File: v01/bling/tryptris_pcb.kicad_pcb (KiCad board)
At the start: 2 copper layers, 298.8 x 122 mm, 217 parts, among them J1 USB_C_Receptacle_USB2.0, J2 I2C-L, J3 I2C-R, SW1 Reset, U1 ATmega32U4-AU, U2 MCP23017_SO, U3 IS31FL3733-TQ, U4 HOLE, U4 IS31FL3733-TQ, Y1 16Mhz

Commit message: Add RGB specific silk screens
Don't want to silkscreen over the RGB holes. Also remove some cruft.
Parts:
- removed the G*** at (100.2, 88.0)
- added G***: LOGO, v01:constellation-right-rgb, B.Cu at (251.4, 88.2)
- added G***: LOGO, v01:constellation-left-rgb, B.Cu at (100.5, 88.5)
- moved G*** 152.1 mm to (398.4, 125.7)

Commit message: Remove redundant silk screen.
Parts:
- removed the G*** at (398.4, 125.7)

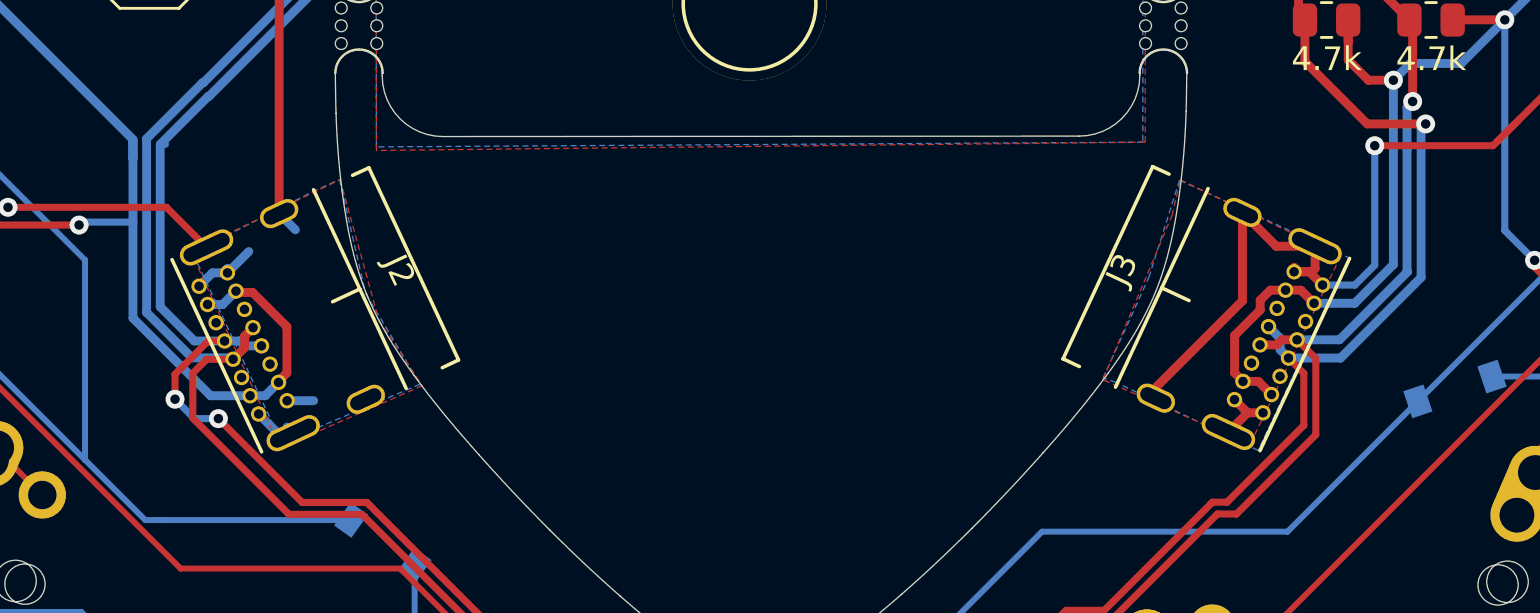
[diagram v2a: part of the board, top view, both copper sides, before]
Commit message: Move interconnect ports
I got some feedback that they might be tight for some cables. By sliding
the ports down a bit they can stay at the same angle and also give more
space for cable housing.
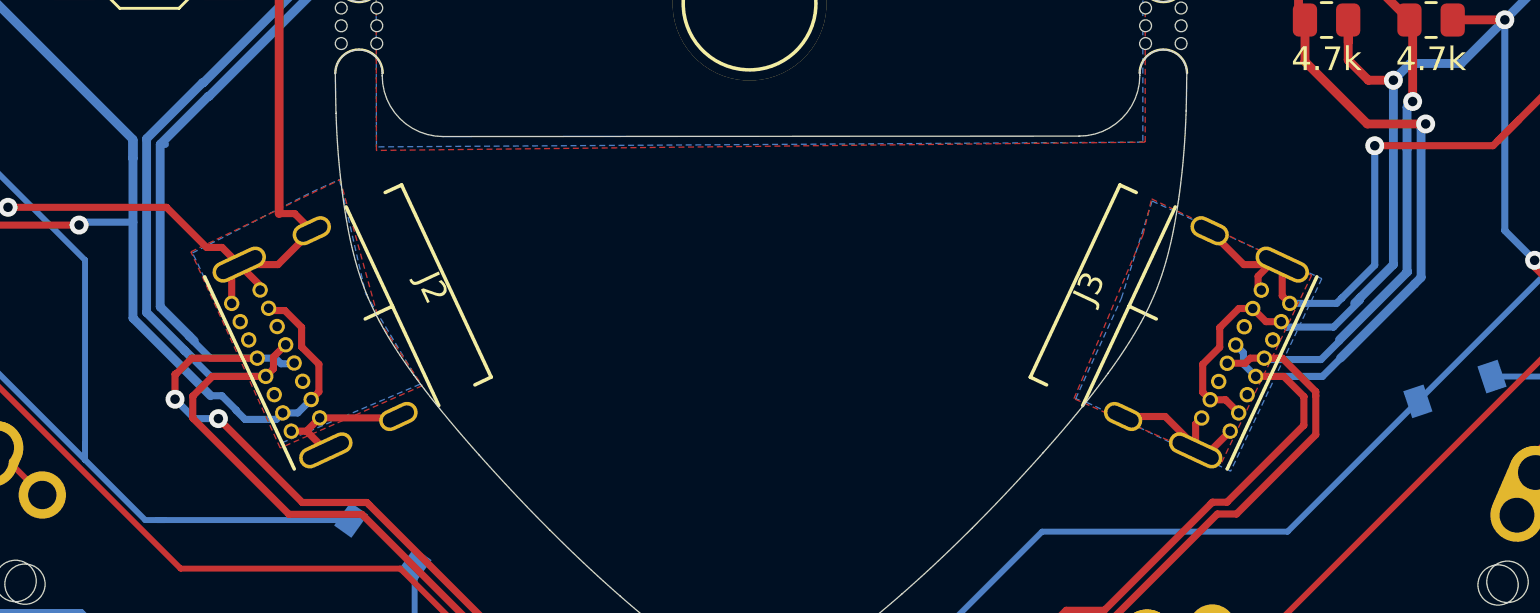
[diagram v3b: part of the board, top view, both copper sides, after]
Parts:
- moved J3 1.59 mm to (191.5, 114.5)
- moved J2 1.56 mm to (160.4, 114.5)
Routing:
- net GND: track 305.6 -> 314.6 mm
- net VSS: track 205.6 -> 202.5 mm
- net SCL-L: track 171.3 -> 174.3 mm
- net SDA-L: track 161.7 -> 164.2 mm
- net VBUS: track 217.4 -> 219.6 mm
- net SCL-R: track 163.2 -> 165.4 mm
- net SDA-R: track 154.0 -> 156.1 mm

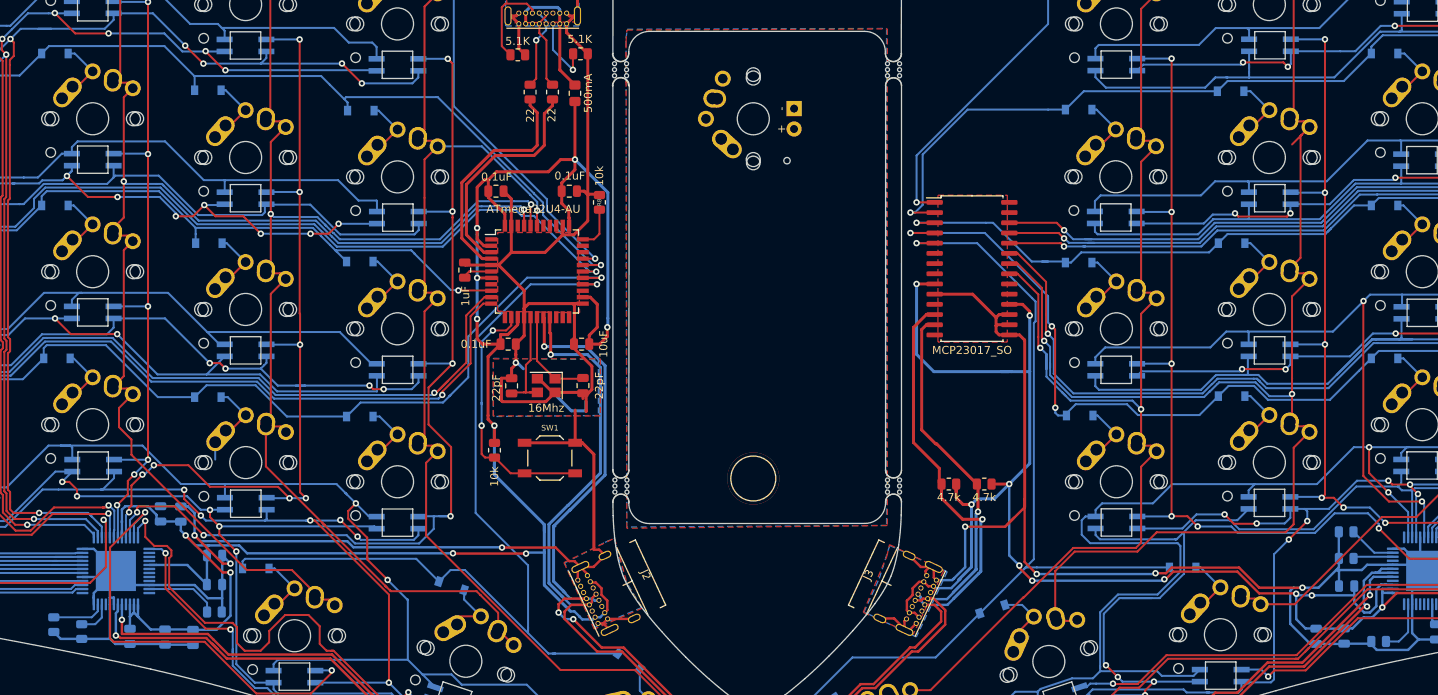
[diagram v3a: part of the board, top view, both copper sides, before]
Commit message: Move RGB LED footprint to a local lib
I don't want as much content on the silkscreen.
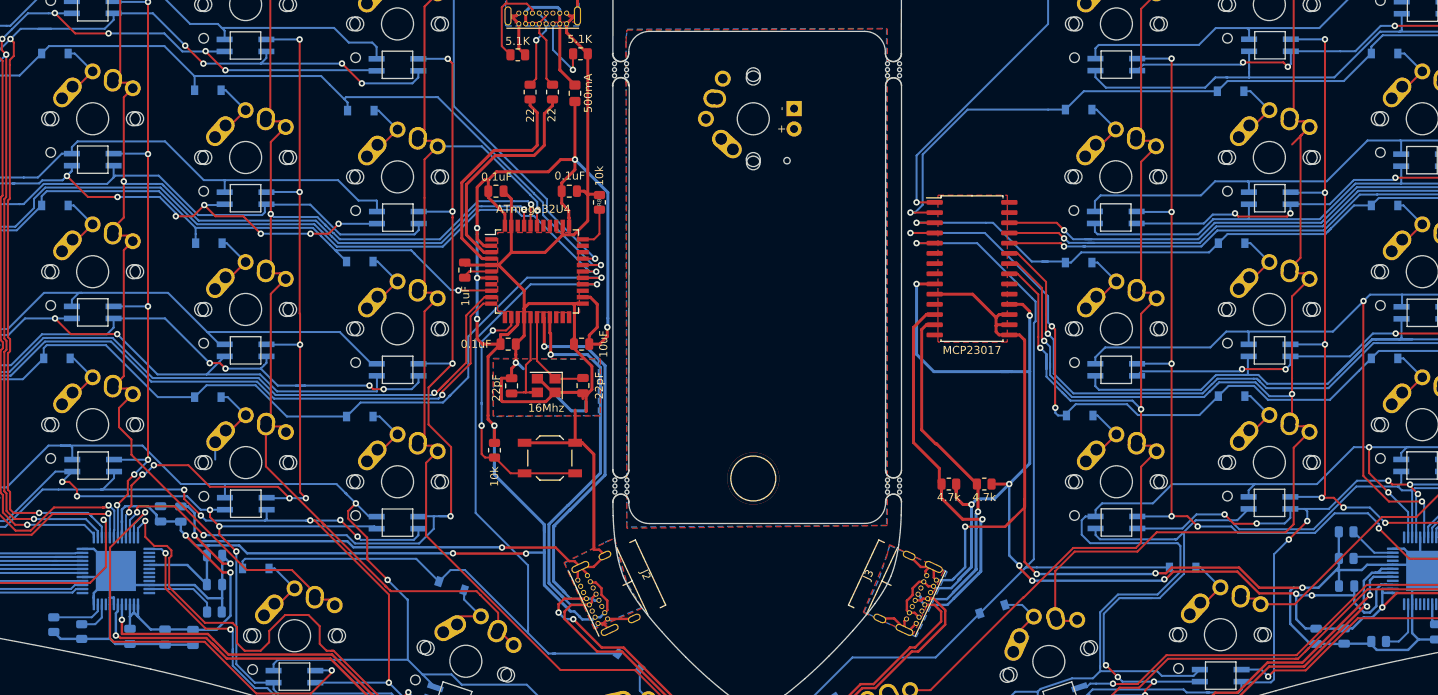
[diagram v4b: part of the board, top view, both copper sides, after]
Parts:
- D100, D101, D102, D103, D104, D105, D106, D107, D108, D55, D56, D57, D58, D59, D60, D61, D62, D63, D64, D65, D66, D67, D68, D69, D70, D71, D72, D73, D74, D75, D76, D77, D78, D79, D80, D81, D82, D83, D84, D85, D86, D87, D88, D89, D90, D91, D92, D93, D94, D95, D96, D97, D98, D99: footprint Keebio-Parts:RGB_3528_Blue_Notch-MX -> v01:RGB_3528_Blue_Notch-MX
- U1: value ATmega32U4-AU -> ATmega32U4
- U2: value MCP23017_SO -> MCP23017

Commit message: Add mounting holes to bling.
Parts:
- added REF**: MountingHole_2.2mm_M2_DIN965_Pad, MountingHole:MountingHole_2.2mm_M2_DIN965_Pad, F.Cu at (161.9, 123.0)
- added REF**: MountingHole_2.2mm_M2_DIN965_Pad, MountingHole:MountingHole_2.2mm_M2_DIN965_Pad, F.Cu at (190.2, 123.1)
- added REF**: MountingHole_2.2mm_M2_DIN965_Pad, MountingHole:MountingHole_2.2mm_M2_DIN965_Pad, F.Cu at (208.9, 54.6)
- added REF**: MountingHole_2.2mm_M2_DIN965_Pad, MountingHole:MountingHole_2.2mm_M2_DIN965_Pad, F.Cu at (143.0, 54.6)
- added REF**: MountingHole_2.2mm_M2_DIN965_Pad, MountingHole:MountingHole_2.2mm_M2_DIN965_Pad, F.Cu at (268.5, 118.8)
- added REF**: MountingHole_2.2mm_M2_DIN965_Pad, MountingHole:MountingHole_2.2mm_M2_DIN965_Pad, F.Cu at (83.8, 118.8)
- added REF**: MountingHole_2.2mm_M2_DIN965_Pad, MountingHole:MountingHole_2.2mm_M2_DIN965_Pad, F.Cu at (306.3, 37.6)
- added REF**: MountingHole_2.2mm_M2_DIN965_Pad, MountingHole:MountingHole_2.2mm_M2_DIN965_Pad, F.Cu at (45.7, 37.5)
- moved D27 9.36 mm to (167.5, 130.0)
- moved C9 5.27 mm to (273.2, 117.4)
- moved C15 5.27 mm to (276.6, 117.4)
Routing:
- net VBUS: track 219.6 -> 232.5 mm, vias 14 -> 12
- net Row4-L: track 113.4 -> 124.1 mm
- net VSS: track 202.5 -> 210.6 mm
- net Net-(D27-Pad2): track 9.48 -> 12.5 mm
- net Row1-R: track 141.1 -> 142.2 mm

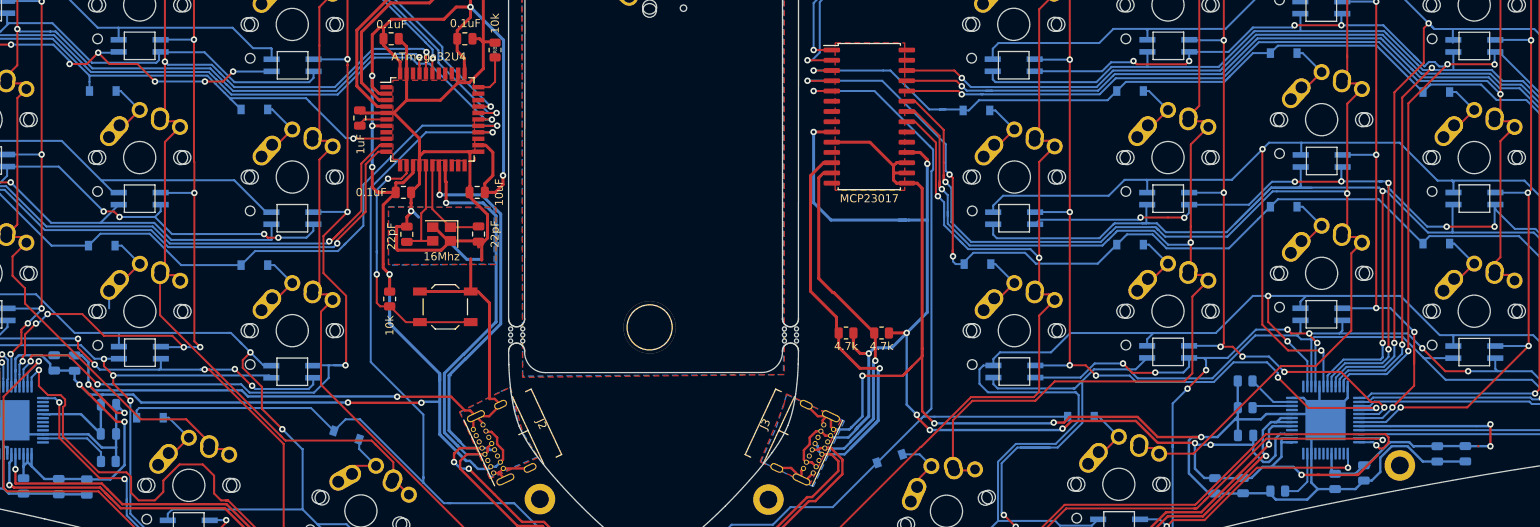
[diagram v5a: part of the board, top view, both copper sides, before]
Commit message: Make schematic clearer
* Improve routing around mounting holes
* Fix all DRC errors.
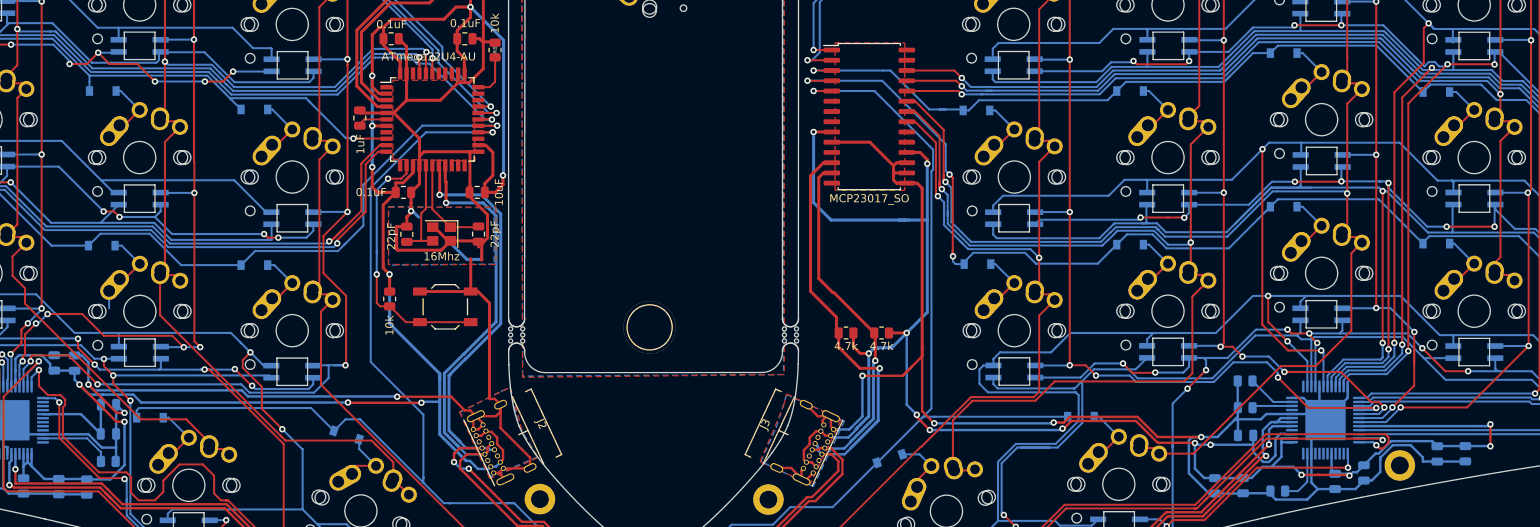
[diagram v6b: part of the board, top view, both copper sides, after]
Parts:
- U1: value ATmega32U4 -> ATmega32U4-AU
- U2: value MCP23017 -> MCP23017_SO
- turned C12 to 270 degrees
- turned C15 to 90 degrees
- turned C18 to 270 degrees
- turned C9 to 90 degrees
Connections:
- C12 pad 1: +5V -> GND
- C12 pad 2: GND -> +5V
- C15 pad 1: VBUS -> VSS
- C15 pad 2: VSS -> VBUS
- C18 pad 1: +5V -> GND
- C18 pad 2: GND -> +5V
- C9 pad 1: VBUS -> VSS
- C9 pad 2: VSS -> VBUS
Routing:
- net GND: track 314.6 -> 325.9 mm
- net VBUS: track 232.5 -> 227.7 mm, vias 12 -> 13
- net +5V: track 262.0 -> 263.4 mm
- net VSS: track 210.6 -> 211.3 mm
